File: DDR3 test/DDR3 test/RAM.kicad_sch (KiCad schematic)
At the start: 0 parts

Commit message: Added libraries to local project path and imported DDR3
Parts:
- added U7: MT41K256M16TW-107:P, footprint:FBGA96_8X14_MRN, symbol Personal:MT41K256M16TW-107_P

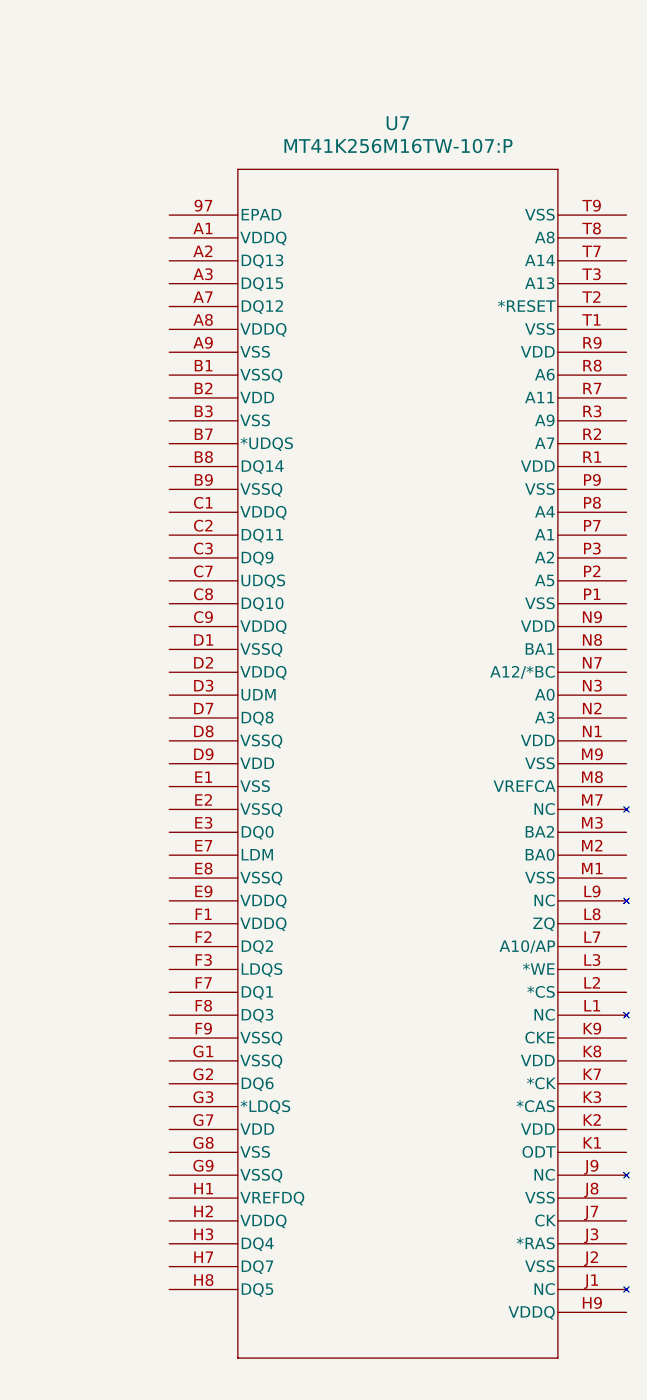
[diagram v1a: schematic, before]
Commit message: group ddr pins by function in symbol
group ddr pins by function in symbol
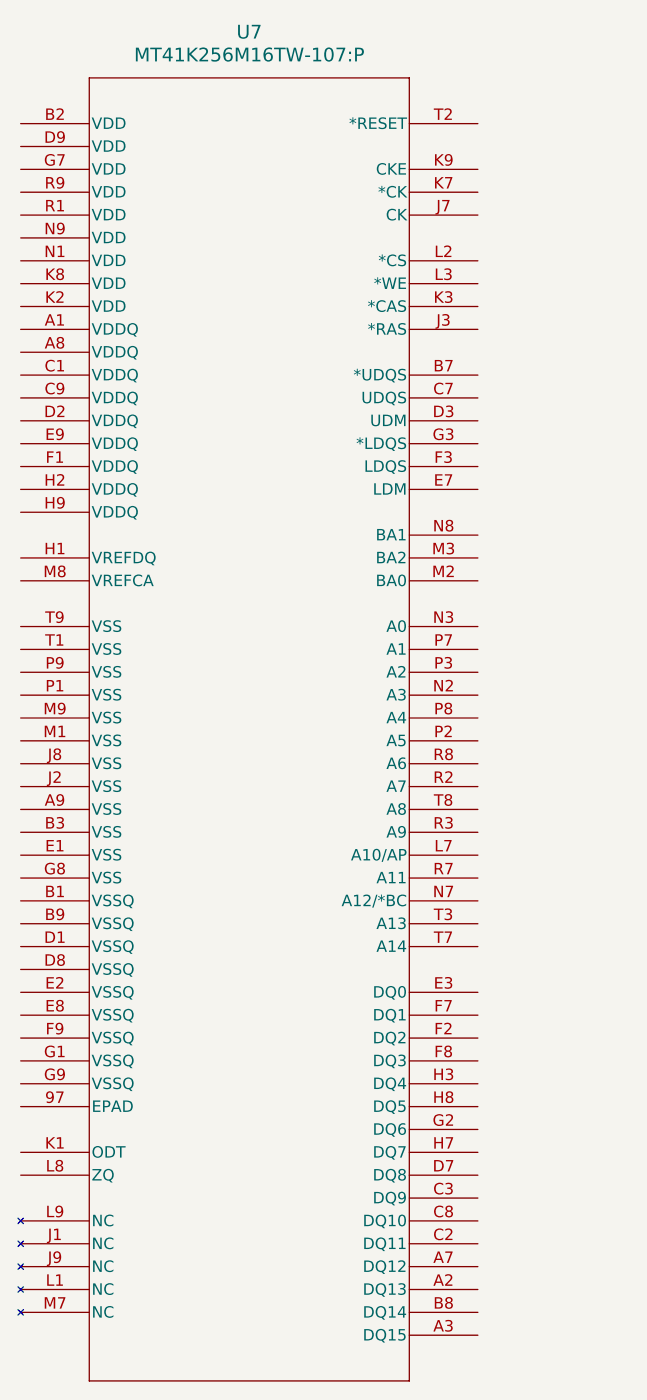
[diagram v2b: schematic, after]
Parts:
- U7: footprint footprint:FBGA96_8X14_MRN -> FBGA96_8X14_MRN
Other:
- moved on the sheet: U7
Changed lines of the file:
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@@
 	(symbol
 		(lib_id "Personal:MT41K256M16TW-107_P")
-		(at 45.72 45.72 0)
+		(at 29.21 35.56 0)
 		(unit 1)
 		(exclude_from_sim no)
@@
 		(fields_autoplaced yes)
 		(property "Reference" "U7"
-			(at 71.12 35.56 0)
+			(at 54.61 25.4 0)
 			(effects
 				(font
@@
 		)
 		(property "Value" "MT41K256M16TW-107:P"
-			(at 71.12 38.1 0)
+			(at 54.61 27.94 0)
 			(effects
 				(font
@@
 			)
 		)
-		(property "Footprint" "footprint:FBGA96_8X14_MRN"
-			(at 45.72 45.72 0)
+		(property "Footprint" "FBGA96_8X14_MRN"
+			(at 29.21 35.56 0)
 			(effects
 				(font
@@
 		)
 		(property "Datasheet" "MT41K256M16TW-107:P"
-			(at 45.72 45.72 0)
+			(at 29.21 35.56 0)
 			(effects
 				(font
@@
 		)
 		(property "Description" ""
-			(at 45.72 45.72 0)
+			(at 29.21 35.56 0)
 			(effects
 				(font

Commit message: Resistor Footprints
- Fixed resistor footprints
- Re-added 3D models
- Routed 1.5V reg
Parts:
- U7: footprint FBGA96_8X14_MRN -> Sync_VT extras:FBGA96_8X14_MRN
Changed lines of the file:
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@@
 			)
 		)
-		(property "Footprint" "FBGA96_8X14_MRN"
+		(property "Footprint" "Sync_VT extras:FBGA96_8X14_MRN"
 			(at 29.21 35.56 0)
 			(effects

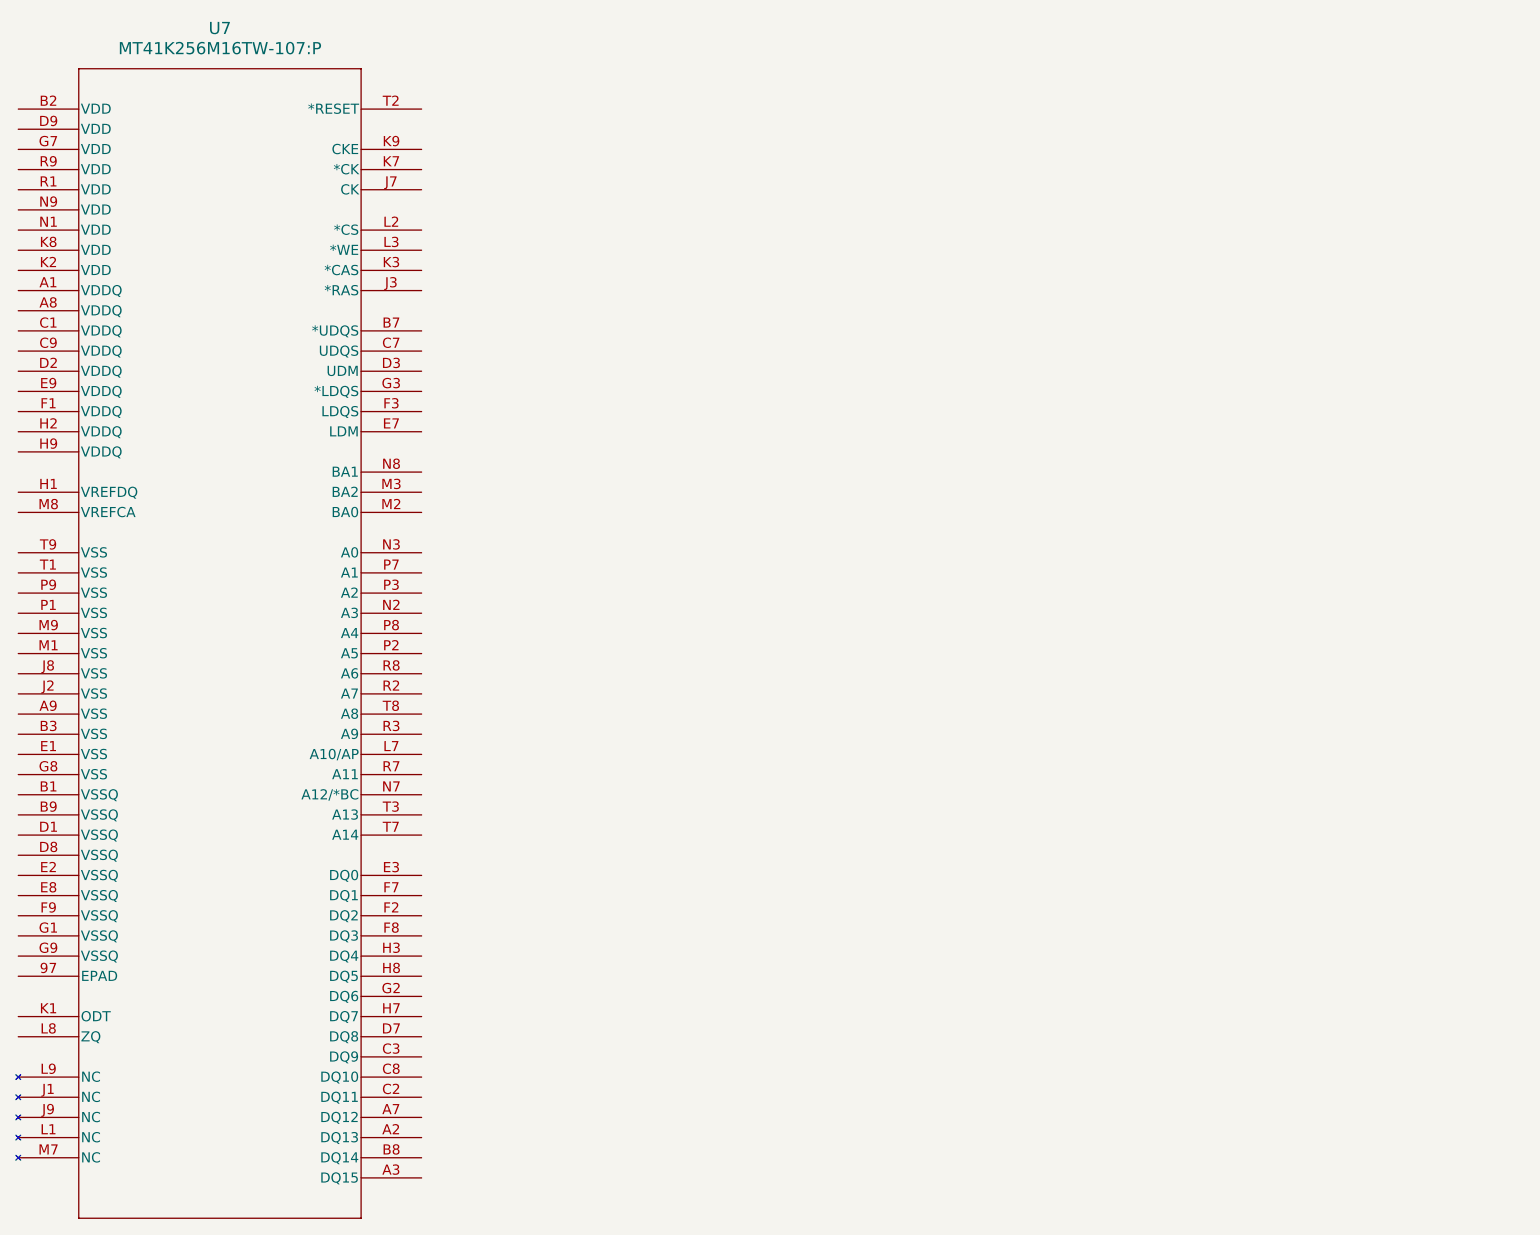
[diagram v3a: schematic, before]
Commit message: pin assignments
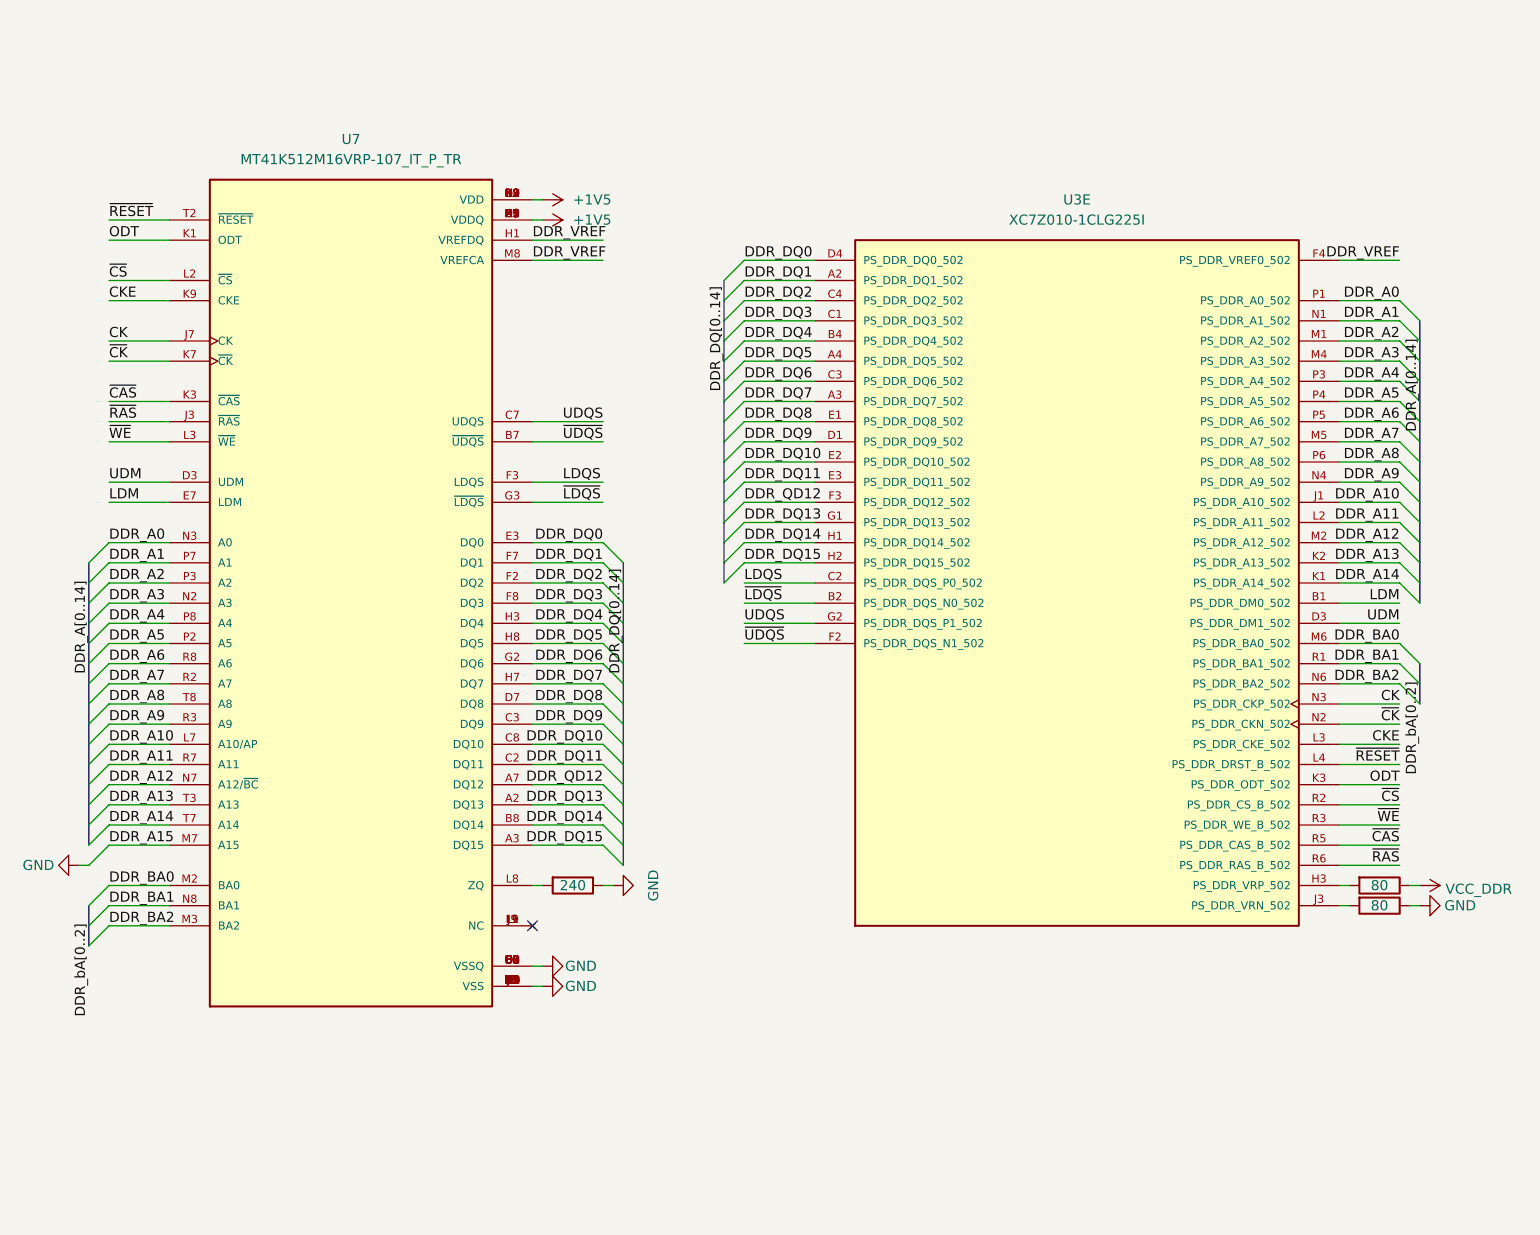
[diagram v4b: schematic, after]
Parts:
- removed U7: MT41K256M16TW-107:P, Sync_VT extras:FBGA96_8X14_MRN, symbol Personal:MT41K256M16TW-107_P
- added R32: 240, Resistor_SMD:R_0402_1005Metric, symbol Device:R
- added R33, R34: 80, Resistor_SMD:R_0402_1005Metric, symbol Device:R
- added U3: XC7Z010-1CLG225I, Sync_VT extras:BGA225C80P15X15_1300X1300X150N, symbol Personal:XC7Z010-1CLG225I
- added U7: MT41K512M16VRP-107_IT_P_TR, Sync_VT extras:IC_MT41K512M16VRP-107_IT_P_TR, symbol Personal:MT41K512M16VRP-107_IT_P_TR
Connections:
- new net: R33.2, U3.H3 (PS_DDR_VRP_502)
- new net: R34.2, U3.J3 (PS_DDR_VRN_502)
- new net: U7.J1 (NC), U7.J9 (NC), U7.L1 (NC), U7.L9 (NC)
- new net: R32.2, U7.L8 (ZQ)
- new net +1V5: U7.A1 (VDDQ), U7.A8 (VDDQ), U7.B2 (VDD), U7.C1 (VDDQ), U7.C9 (VDDQ), U7.D2 (VDDQ), U7.D9 (VDD), U7.E9 (VDDQ), U7.F1 (VDDQ), U7.G7 (VDD), U7.H2 (VDDQ), U7.H9 (VDDQ), U7.K2 (VDD), U7.K8 (VDD), U7.N1 (VDD), U7.N9 (VDD), U7.R1 (VDD), U7.R9 (VDD)
- new net CK: U3.N3 (PS_DDR_CKP_502), U7.J7 (CK)
- new net CKE: U3.L3 (PS_DDR_CKE_502), U7.K9 (CKE)
- new net DDR_A0: U3.P1 (PS_DDR_A0_502), U7.N3 (A0)
- new net DDR_A1: U3.N1 (PS_DDR_A1_502), U7.P7 (A1)
- new net DDR_A10: U3.J1 (PS_DDR_A10_502), U7.L7 (A10/AP)
- new net DDR_A11: U3.L2 (PS_DDR_A11_502), U7.R7 (A11)
- new net DDR_A12: U3.M2 (PS_DDR_A12_502), U7.N7 (A12/~{BC})
- new net DDR_A13: U3.K2 (PS_DDR_A13_502), U7.T3 (A13)
- new net DDR_A14: U3.K1 (PS_DDR_A14_502), U7.T7 (A14)
- new net DDR_A2: U3.M1 (PS_DDR_A2_502), U7.P3 (A2)
- new net DDR_A3: U3.M4 (PS_DDR_A3_502), U7.N2 (A3)
- new net DDR_A4: U3.P3 (PS_DDR_A4_502), U7.P8 (A4)
- new net DDR_A5: U3.P4 (PS_DDR_A5_502), U7.P2 (A5)
- new net DDR_A6: U3.P5 (PS_DDR_A6_502), U7.R8 (A6)
- new net DDR_A7: U3.M5 (PS_DDR_A7_502), U7.R2 (A7)
- new net DDR_A8: U3.P6 (PS_DDR_A8_502), U7.T8 (A8)
- new net DDR_A9: U3.N4 (PS_DDR_A9_502), U7.R3 (A9)
- new net DDR_BA0: U3.M6 (PS_DDR_BA0_502), U7.M2 (BA0)
- new net DDR_BA1: U3.R1 (PS_DDR_BA1_502), U7.N8 (BA1)
- new net DDR_BA2: U3.N6 (PS_DDR_BA2_502), U7.M3 (BA2)
- new net DDR_DQ0: U3.D4 (PS_DDR_DQ0_502), U7.E3 (DQ0)
- new net DDR_DQ1: U3.A2 (PS_DDR_DQ1_502), U7.F7 (DQ1)
- new net DDR_DQ10: U3.E2 (PS_DDR_DQ10_502), U7.C8 (DQ10)
- new net DDR_DQ11: U3.E3 (PS_DDR_DQ11_502), U7.C2 (DQ11)
- new net DDR_DQ13: U3.G1 (PS_DDR_DQ13_502), U7.A2 (DQ13)
- new net DDR_DQ14: U3.H1 (PS_DDR_DQ14_502), U7.B8 (DQ14)
- new net DDR_DQ15: U3.H2 (PS_DDR_DQ15_502), U7.A3 (DQ15)
- new net DDR_DQ2: U3.C4 (PS_DDR_DQ2_502), U7.F2 (DQ2)
- new net DDR_DQ3: U3.C1 (PS_DDR_DQ3_502), U7.F8 (DQ3)
- new net DDR_DQ4: U3.B4 (PS_DDR_DQ4_502), U7.H3 (DQ4)
- new net DDR_DQ5: U3.A4 (PS_DDR_DQ5_502), U7.H8 (DQ5)
- new net DDR_DQ6: U3.C3 (PS_DDR_DQ6_502), U7.G2 (DQ6)
- new net DDR_DQ7: U3.A3 (PS_DDR_DQ7_502), U7.H7 (DQ7)
- new net DDR_DQ8: U3.E1 (PS_DDR_DQ8_502), U7.D7 (DQ8)
- new net DDR_DQ9: U3.D1 (PS_DDR_DQ9_502), U7.C3 (DQ9)
- new net DDR_QD12: U3.F3 (PS_DDR_DQ12_502), U7.A7 (DQ12)
- new net DDR_VREF: U3.F4 (PS_DDR_VREF0_502), U7.H1 (VREFDQ), U7.M8 (VREFCA)
- new net GND: R32.1, R34.1, U7.A9 (VSS), U7.B1 (VSSQ), U7.B3 (VSS), U7.B9 (VSSQ), U7.D1 (VSSQ), U7.D8 (VSSQ), U7.E1 (VSS), U7.E2 (VSSQ), U7.E8 (VSSQ), U7.F9 (VSSQ), U7.G1 (VSSQ), U7.G8 (VSS), U7.G9 (VSSQ), U7.J2 (VSS), U7.J8 (VSS), U7.M1 (VSS), U7.M7 (A15), U7.M9 (VSS), U7.P1 (VSS), U7.P9 (VSS), U7.T1 (VSS), U7.T9 (VSS)
- new net LDM: U3.B1 (PS_DDR_DM0_502), U7.E7 (LDM)
- new net LDQS: U3.C2 (PS_DDR_DQS_P0_502), U7.F3 (LDQS)
- new net ODT: U3.K3 (PS_DDR_ODT_502), U7.K1 (ODT)
- new net UDM: U3.D3 (PS_DDR_DM1_502), U7.D3 (UDM)
- new net UDQS: U3.G2 (PS_DDR_DQS_P1_502), U7.C7 (UDQS)
- new net VCC_DDR: R33.1
- new net ~{CAS}: U3.R5 (PS_DDR_CAS_B_502), U7.K3 (~{CAS})
- new net ~{CK}: U3.N2 (PS_DDR_CKN_502), U7.K7 (~{CK})
- new net ~{CS}: U3.R2 (PS_DDR_CS_B_502), U7.L2 (~{CS})
- new net ~{LDQS}: U3.B2 (PS_DDR_DQS_N0_502), U7.G3 (~{LDQS})
- new net ~{RAS}: U3.R6 (PS_DDR_RAS_B_502), U7.J3 (~{RAS})
- new net ~{RESET}: U3.L4 (PS_DDR_DRST_B_502), U7.T2 (~{RESET})
- new net ~{UDQS}: U3.F2 (PS_DDR_DQS_N1_502), U7.B7 (~{UDQS})
- new net ~{WE}: U3.R3 (PS_DDR_WE_B_502), U7.L3 (~{WE})
- no-connect marks 0 -> 1
